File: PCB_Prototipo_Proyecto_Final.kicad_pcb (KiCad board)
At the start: 2 copper layers, 165.1 x 154.9 mm, 152 parts, among them IC1 UA741CP, J1 VIN, J10 Terminal_Sensores_Nivel, J11 Terminal_Sensor_Flujo, J12 Rele_4, J13 Rele_7, J14 Rele_1, J15 Rele_5, J16 Rele_2, J17 Rele_3, J18 Rele_6, J19 Pin GND, J2 Conn_01x15, J20 Conector 3V3, J21 Conector GND, J22 Pin_3V3, J23 Pin_3V3, J24 Pin GND, J25 Pin_3V3, J26 Pin GND, J27 Pin_3V3, J28 Pin_3V3, J29 Pin_3V3, J3 Conn_01x15, J30 Pin GND, J31 Pin GND, J32 Pin GND, J33 Pin GND, J34 Pin GND, J35 Pin GND, J36 Pin GND, J37 Pin GND, J38 Pin GND, J39 Pin GND, J4 Terminal_Sensor_pH, J40 Pin GND, J41 Pin GND, J42 Pin GND, J43 Conector GND, J5 Terminal_Sensor_CO2, J6 Terminal_Sensor_TDS, J7 Terminal_Sensor_Temp_Sumerg, J8 Terminal_Sensor_Iluminacion, J9 Terminal_Sensor_Temp_y_Hum, K1 SRD-05VDC-SL-C, K2 SRD-05VDC-SL-C, K3 SRD-05VDC-SL-C, K4 SRD-05VDC-SL-C, K5 SRD-05VDC-SL-C, K6 SRD-05VDC-SL-C, K7 SRD-05VDC-SL-C, Q1 2N7002, Q10 2N7002, Q11 2N7002, Q12 2N7002, Q13 2N7002, Q14 2N7002, Q15 2N7002, Q2 2N7002, Q3 2N7002, Q4 2N7002, Q5 2N7002, Q6 2N7002, Q7 2N7002, Q8 2N7002, Q9 2N7002, U1 LM2596S-5, U2 LM1117-3.3, U3 MCP23008-xP

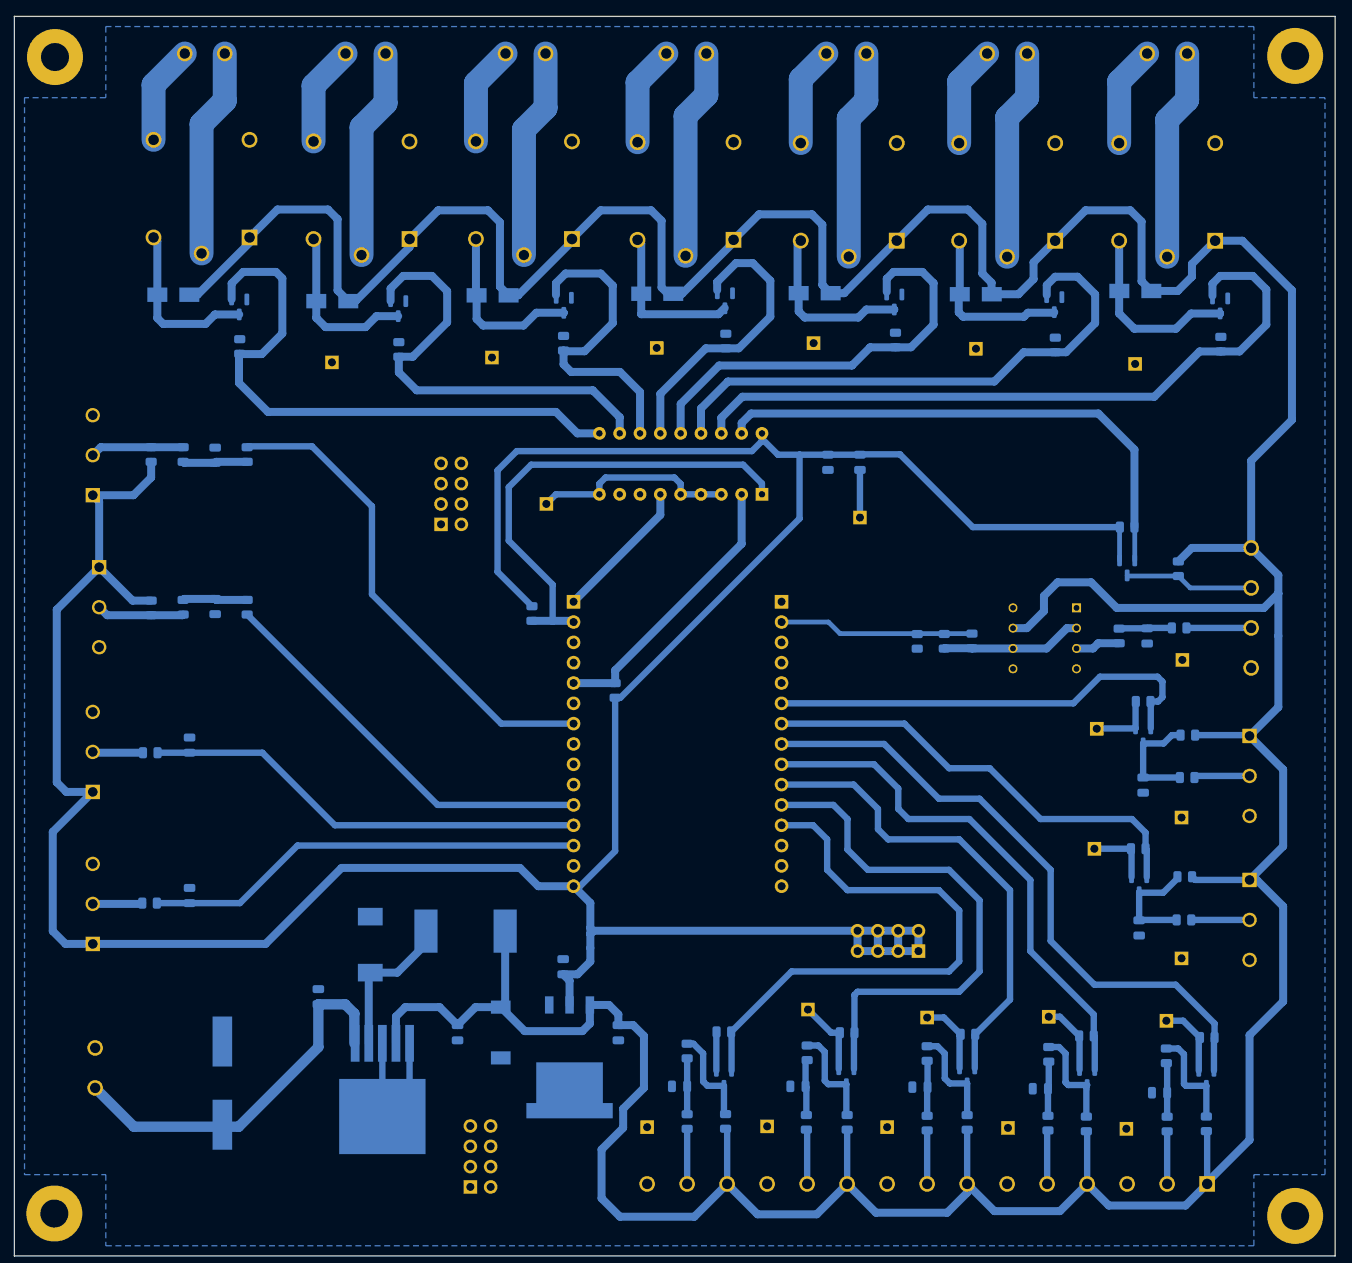
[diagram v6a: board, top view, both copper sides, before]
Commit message: Modificacion de PCB.
Me di cuenta que, al pasar los componentes SMD y las pistas al lado BOTTOM, los componentes TH quedaron todos al revés, por lo que será necesario rediseñar la PCB para acomodarlos del lado TOP correctamente.
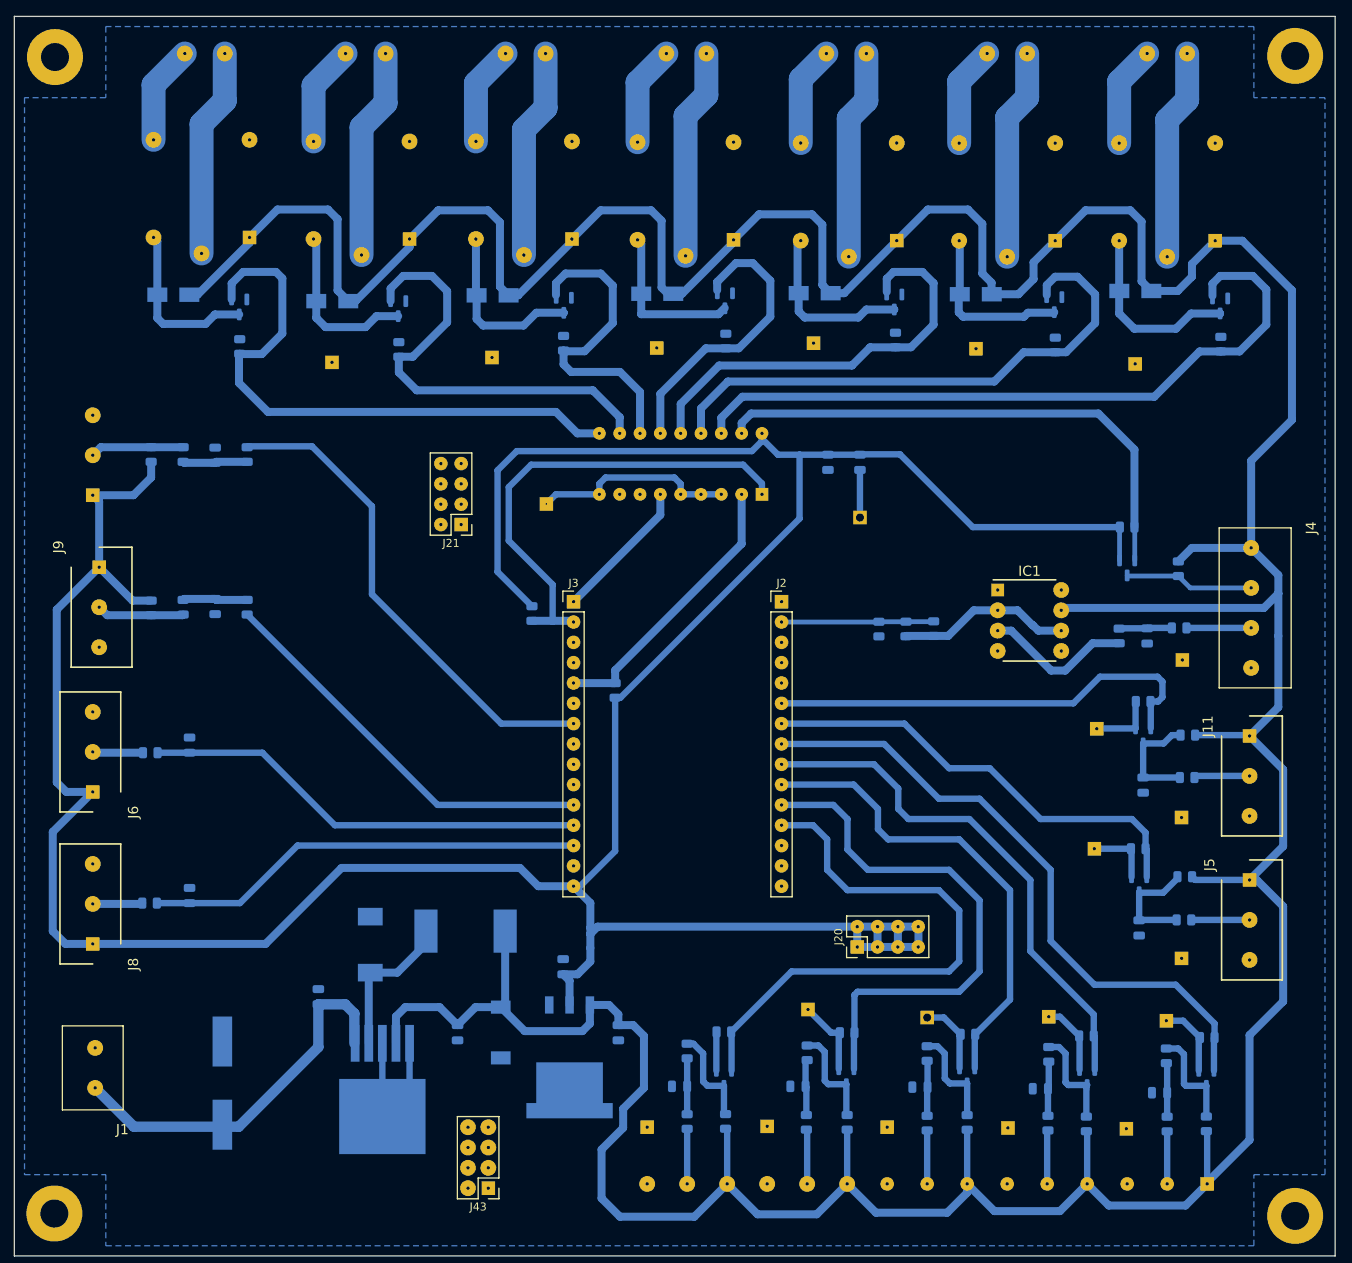
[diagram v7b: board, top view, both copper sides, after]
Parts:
- IC1, J1, J11, J2, J20, J21, J3, J4, J43, J5, J6, J8, J9: moved to F.Cu
- moved J20 7.67 mm to (237.8, 169.7)
- moved R41 5.03 mm to (243.9, 129.9)
- moved R1 5.03 mm to (247.3, 129.9)
- moved R3 5.03 mm to (240.5, 129.9)
- moved IC1 2.94 mm to (259.3, 128.8), turned to 0 degrees
- moved J21 2.52 mm to (188.3, 116.9), turned to 180 degrees
- moved J43 2.25 mm to (191.7, 199.8), turned to 180 degrees
- turned J2 to 0 degrees
- turned J3 to 0 degrees
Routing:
- net Net-(IC1-Pad3): track 5.60 -> 18.7 mm
- net +5V: track 615.4 -> 604.7 mm
- net /Entradas/pH_Analog: track 24.4 -> 19.0 mm
- net Net-(IC1-Pad2): track 17.6 -> 21.8 mm
- net +3.3V: track 463.2 -> 462.3 mm

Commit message: Inicio de rerouteo.
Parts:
- J10, J12, J13, J14, J15, J16, J17, J18, J19, J22, J23, J24, J25, J26, J27, J28, J29, J34, J37, J38, J39, J40, J41, J42, J7, K1, K2, K3, K4, K5, K6, K7, U3: moved to F.Cu
- moved J7 145.4 mm to (287.6, 112.5)
- moved J6 145.2 mm to (287.4, 151.3)
- moved J4 145.2 mm to (141.8, 118.5)
- moved J8 145.1 mm to (287.3, 170.7)
- moved J11 145.0 mm to (141.8, 142.6)
- moved J5 144.9 mm to (141.9, 160.8)
- moved J9 144.8 mm to (287.5, 131.5), turned to 90 degrees
- moved J1 144.7 mm to (287.2, 185.0), turned to -90 degrees
- moved R4 131.3 mm to (280.8, 108.5)
- moved R5 131.2 mm to (280.7, 125.5)
- moved J10 130.5 mm to (151.1, 200.2), turned to 0 degrees
- moved R19 130.4 mm to (279.8, 146.3), turned to 180 degrees
- moved R20 130.3 mm to (279.7, 165.6), turned to 180 degrees
- moved R39 127.7 mm to (151.4, 143.7), turned to 180 degrees
- moved R23 127.5 mm to (151.5, 148.4), turned to 0 degrees
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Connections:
- J10 pad 1: +5V -> GND
- J10 pad 10: +5V -> GND
- J10 pad 11: /Entradas/SensorNivel_4 -> /Entradas/SensorNivel_2
- J10 pad 12: GND -> +5V
- J10 pad 13: +5V -> GND
- J10 pad 14: /Entradas/SensorNivel_5 -> /Entradas/SensorNivel_1
- J10 pad 15: GND -> +5V
- J10 pad 2: /Entradas/SensorNivel_1 -> /Entradas/SensorNivel_5
- J10 pad 3: GND -> +5V
- J10 pad 4: +5V -> GND
- J10 pad 5: /Entradas/SensorNivel_2 -> /Entradas/SensorNivel_4
- J10 pad 6: GND -> +5V
- J10 pad 7: +5V -> GND
- J10 pad 9: GND -> +5V
- J9 pad 1: +3.3V -> GND
- J9 pad 3: GND -> +3.3V
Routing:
- net +5V: track 604.7 -> 147.8 mm
- net +3.3V: track 462.3 -> 67.4 mm
- net /Microcontrolador/Rele_7: track 73.9 -> 0.00 mm
- net /Microcontrolador/SensorNivel_1: track 79.7 -> 12.8 mm
- net /Microcontrolador/Trigger__pH: track 66.6 -> 0.00 mm
- net /Entradas/Data_SensorTempSumerg: track 61.6 -> 0.00 mm
- net /Microcontrolador/MCP23008_SCL: track 59.4 -> 0.00 mm
- net /Microcontrolador/SensorNivel_4: track 67.0 -> 9.31 mm
- net /Microcontrolador/Rele_1: track 88.7 -> 31.5 mm
- net /Microcontrolador/SensorNivel_5: track 72.3 -> 15.6 mm
- net /Microcontrolador/SensorFlujo: track 56.3 -> 0.00 mm
- net /Entradas/TDS_Analog: track 55.8 -> 0.00 mm
- net /Entradas/Ilum_Analog: track 55.1 -> 0.00 mm
- net GND: track 51.3 -> 0.00 mm
- net /Entradas/Data_SensorTempHum: track 50.7 -> 0.00 mm
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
